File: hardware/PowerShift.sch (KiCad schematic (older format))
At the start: 64 parts, among them J1 Barrel_Jack, J10 SHIFT_IN, J11 JST-ZR, J12 JST-ZR, J14 JST-ZR, J2 MICRO_USB, J3 JST-ZR, J4 JST-ZR, J5 SHIFT_IN, J6 SHIFT_IN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

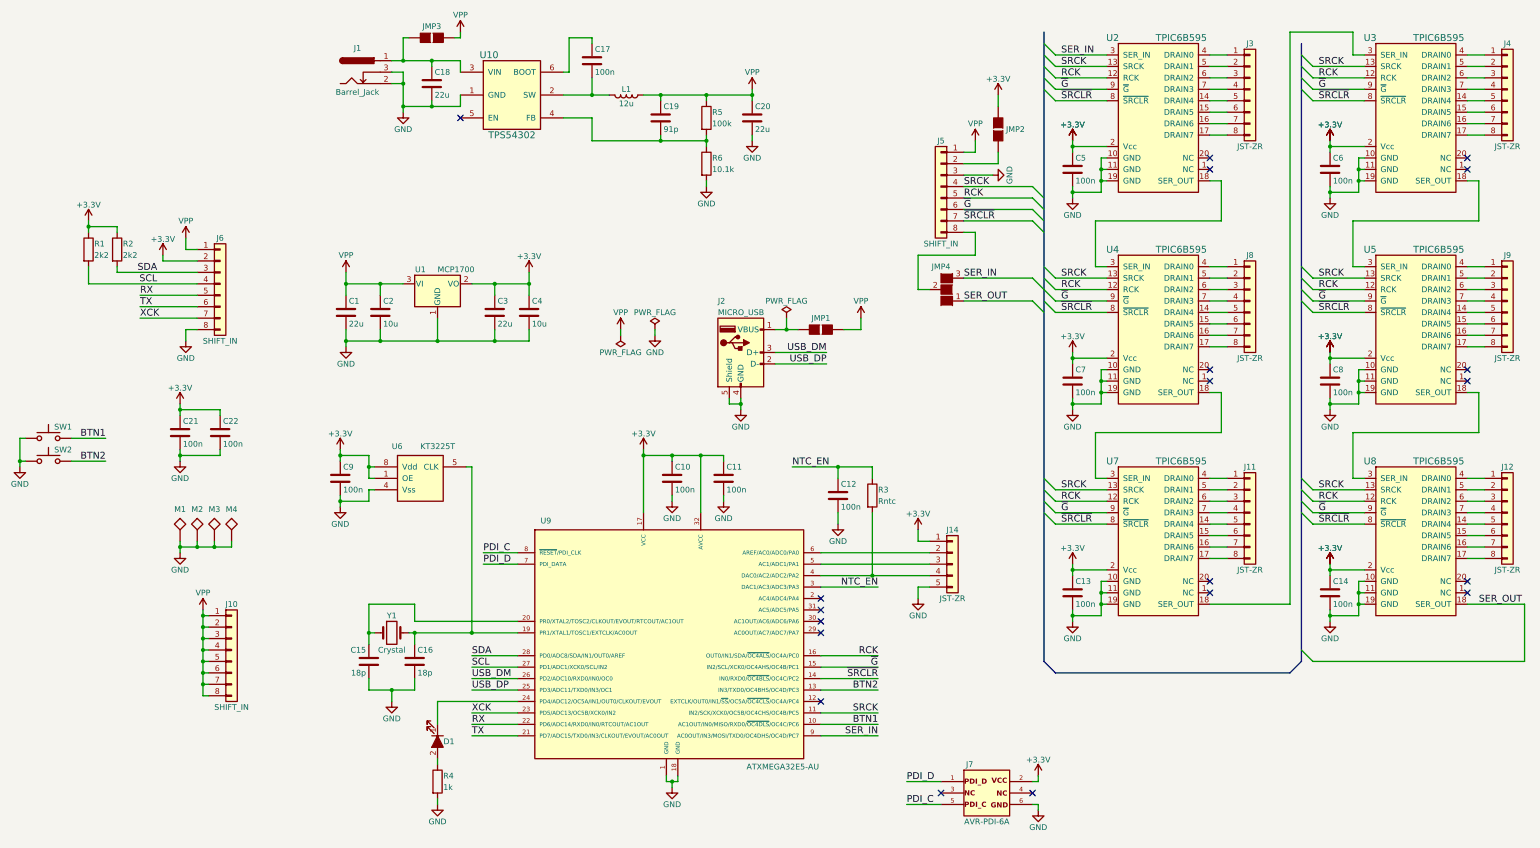
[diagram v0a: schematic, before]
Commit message: Cleaned up schematic layout
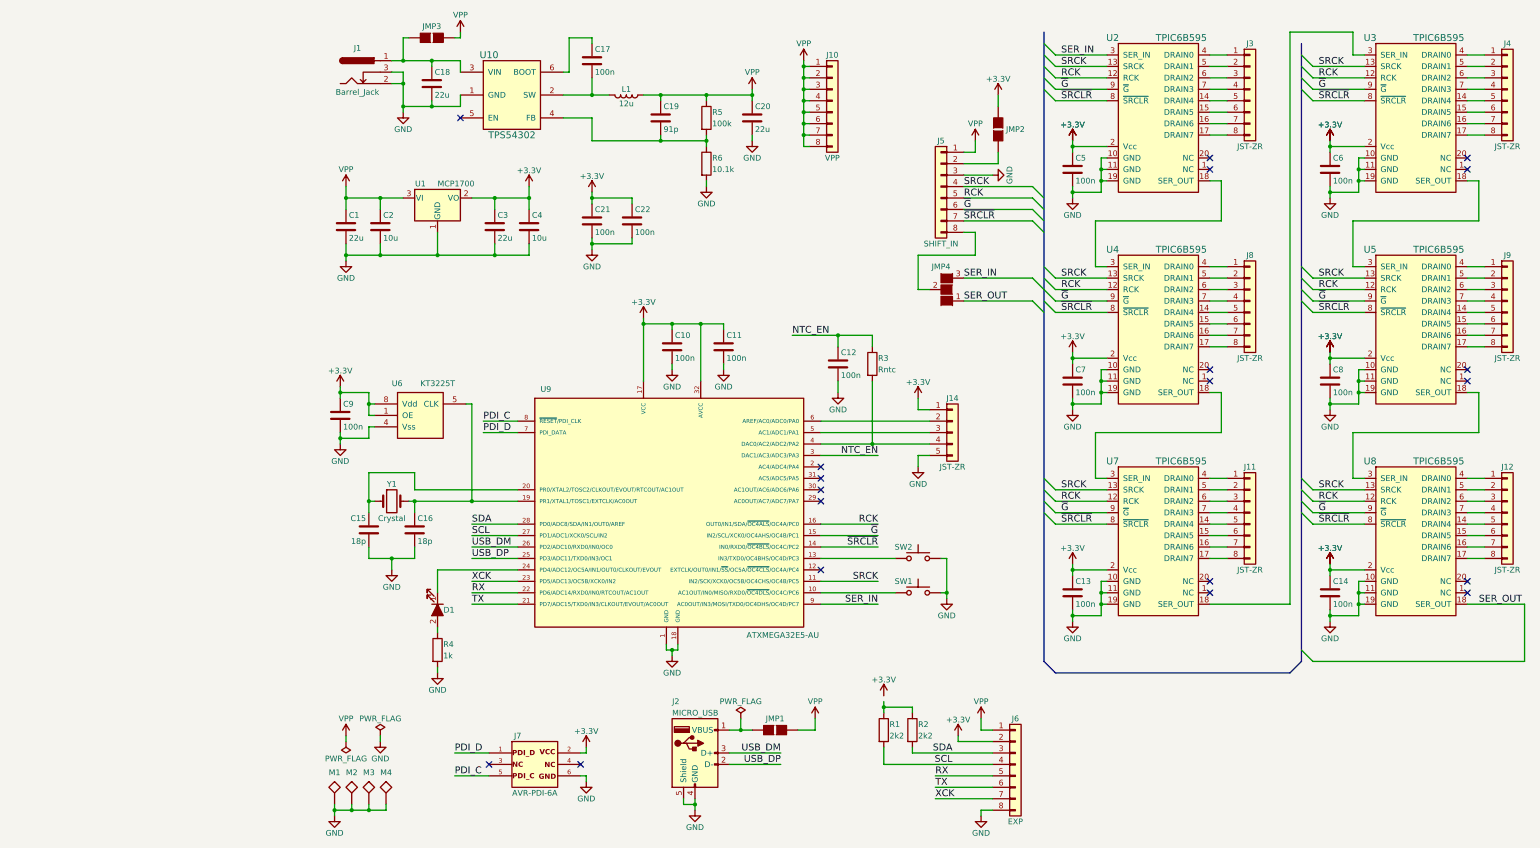
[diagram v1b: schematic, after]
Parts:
- J10: value SHIFT_IN -> VPP
- J6: value SHIFT_IN -> EXP
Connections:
- net +3V3: no longer R1.1, R2.1
- net BTN1: no longer names the net of SW1.2, U9.10 (AC1OUT/IN0/MISO/RXD0/~OC4DLS~/OC4C/PC6)
- net BTN2: no longer names the net of SW2.2, U9.13 (IN3/TXD0/OC4BHS/OC4D/PC3)
- new net: R1.1, R2.1
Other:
- moved on the sheet: C1, C10, C11, C12, C15, C16, C2, C21, C22, C3, C4, C9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

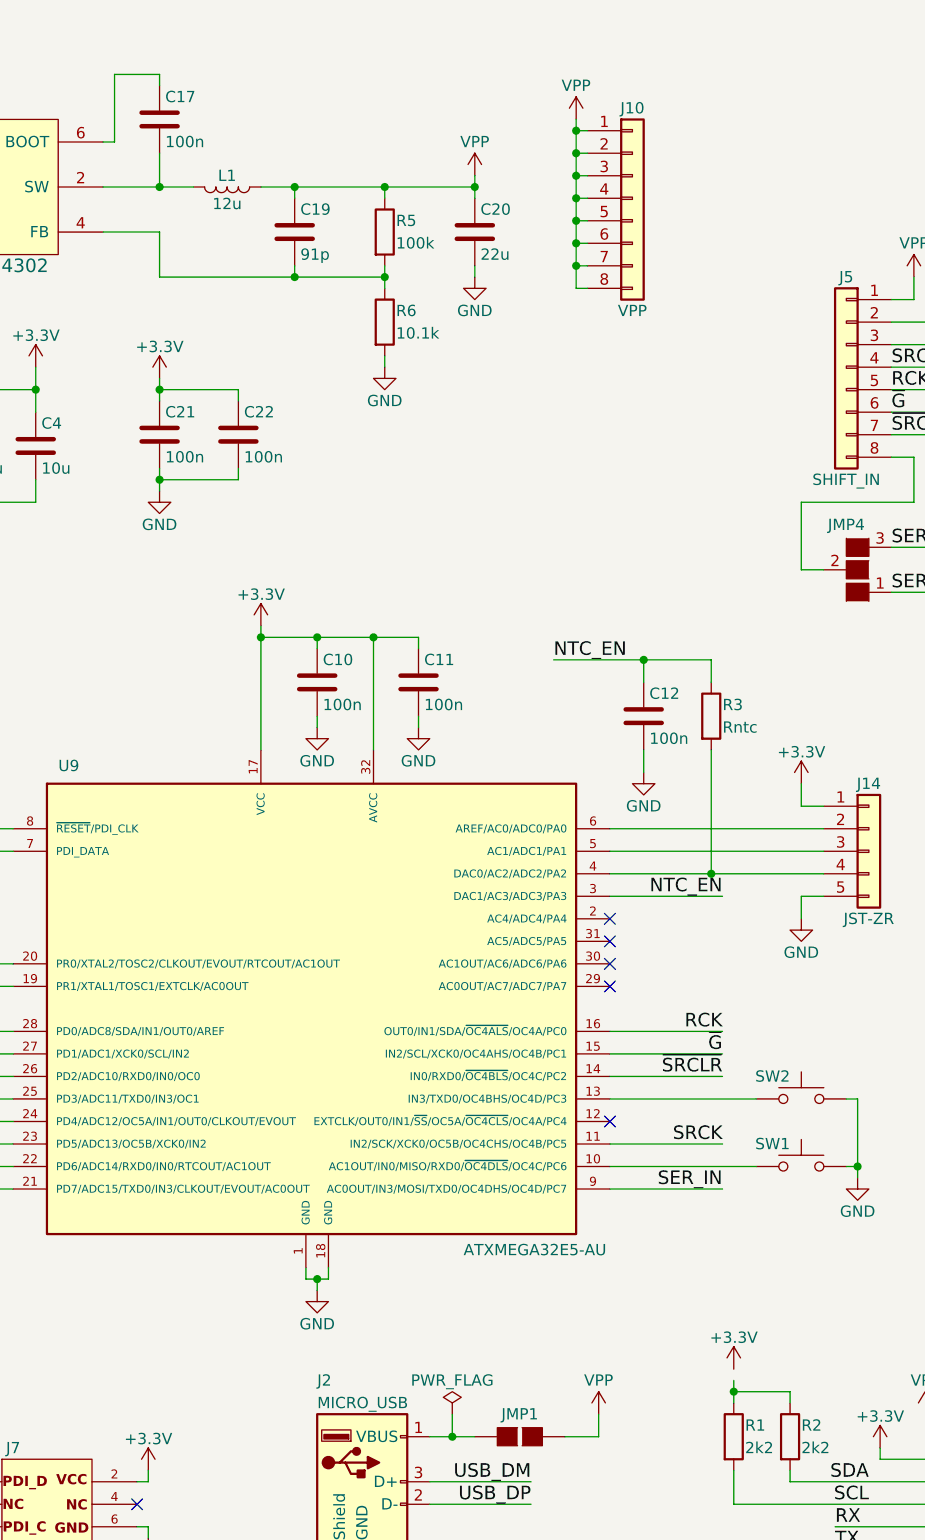
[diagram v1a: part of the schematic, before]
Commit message: Added Vpp voltage switch
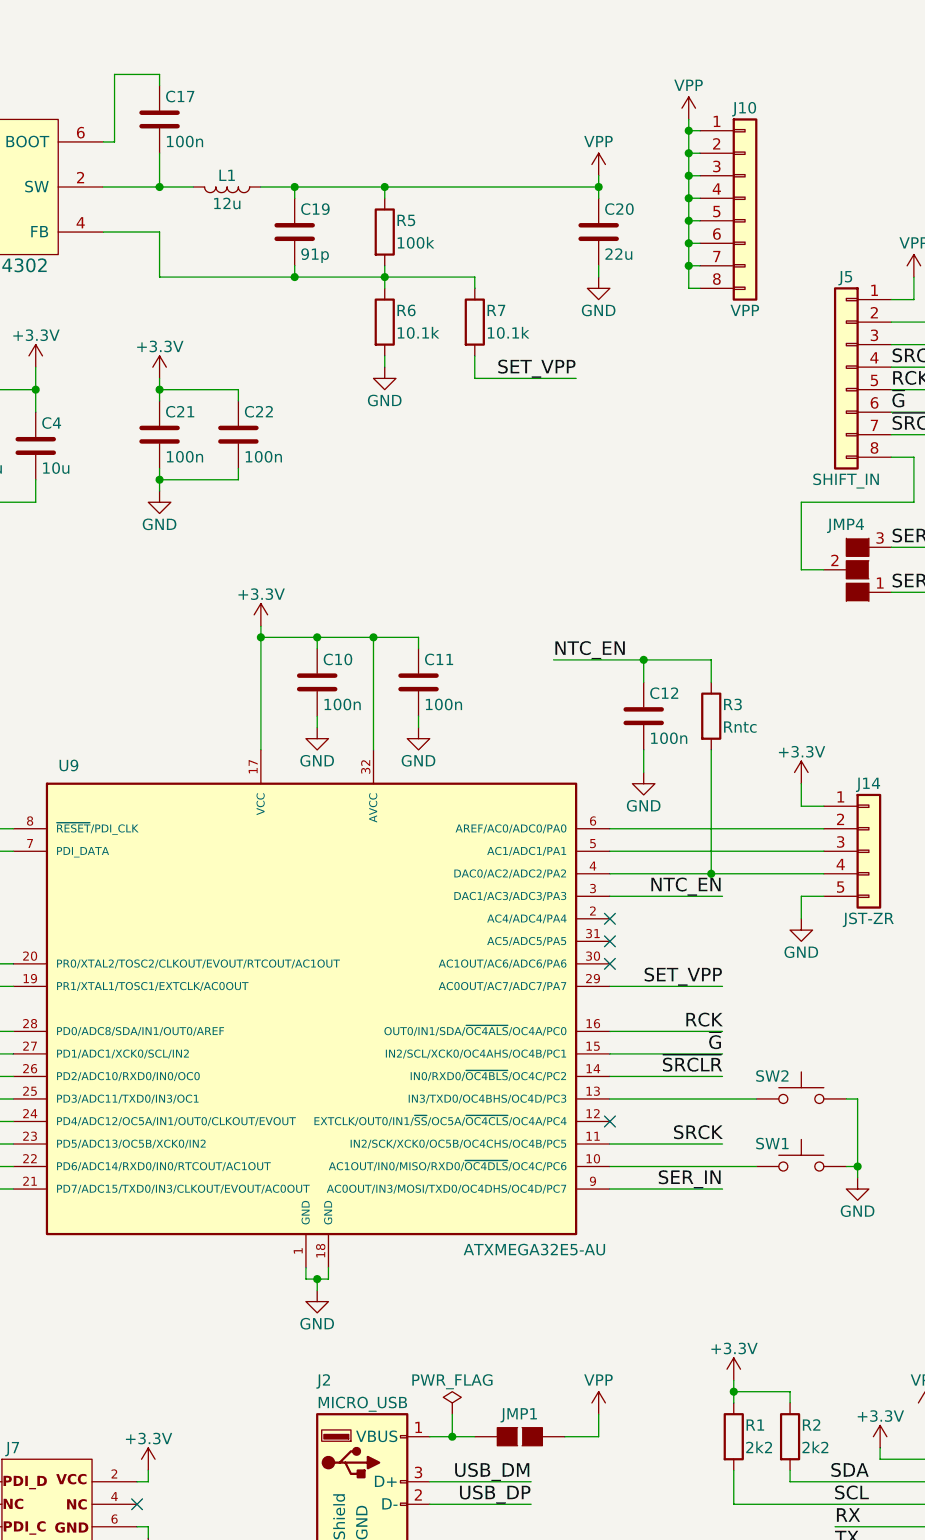
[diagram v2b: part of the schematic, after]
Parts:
- added R7: 10.1k, Resistors_SMD:R_0603_HandSoldering, symbol R
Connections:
- net +3V3: now also R1.1, R2.1
- net SET_VPP: now reaches U9.29 (AC0OUT/AC7/ADC7/PA7)
- net SET_VPP: now also R7.2
- net at C19.2, R5.2, R6.1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: now also R7.1
- no-connect marks 20 -> 19
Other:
- moved on the sheet: C20, J10
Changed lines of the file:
@@
 L VPP #PWR04
 U 1 1 5B2FD383
-P 4250 1200
-F 0 "#PWR04" H 4250 1050 50  0001 C CNN
-F 1 "VPP" H 4250 1350 50  0000 C CNN
-F 2 "" H 4250 1200 50  0001 C CNN
-F 3 "" H 4250 1200 50  0001 C CNN
-	1    4250 1200
+P 4800 1200
+F 0 "#PWR04" H 4800 1050 50  0001 C CNN
+F 1 "VPP" H 4800 1350 50  0000 C CNN
+F 2 "" H 4800 1200 50  0001 C CNN
+F 3 "" H 4800 1200 50  0001 C CNN
+	1    4800 1200
 	1    0    0    -1
 $EndComp
@@
 L +3.3V #PWR038
 U 1 1 5B320992
-P 5400 6500
-F 0 "#PWR038" H 5400 6350 50  0001 C CNN
-F 1 "+3.3V" H 5400 6640 50  0000 C CNN
-F 2 "" H 5400 6500 50  0001 C CNN
-F 3 "" H 5400 6500 50  0001 C CNN
-	1    5400 6500
+P 5400 6550
+F 0 "#PWR038" H 5400 6400 50  0001 C CNN
+F 1 "+3.3V" H 5400 6690 50  0000 C CNN
+F 2 "" H 5400 6550 50  0001 C CNN
+F 3 "" H 5400 6550 50  0001 C CNN
+	1    5400 6550
 	1    0    0    -1
 $EndComp
@@
 NoConn ~ 4850 4600
 NoConn ~ 4850 4700
-NoConn ~ 4850 4800
 NoConn ~ 4850 5400
 Entry Wire Line
@@
 L C C20
 U 1 1 5B314AC7
-P 4250 1450
-F 0 "C20" H 4275 1550 50  0000 L CNN
-F 1 "22u" H 4275 1350 50  0000 L CNN
-F 2 "Capacitors_SMD:C_0805_HandSoldering" H 4288 1300 50  0001 C CNN
-F 3 "" H 4250 1450 50  0001 C CNN
-	1    4250 1450
+P 4800 1450
+F 0 "C20" H 4825 1550 50  0000 L CNN
+F 1 "22u" H 4825 1350 50  0000 L CNN
+F 2 "Capacitors_SMD:C_0805_HandSoldering" H 4838 1300 50  0001 C CNN
+F 3 "" H 4800 1450 50  0001 C CNN
+	1    4800 1450
 	1    0    0    -1
 $EndComp
@@
 Connection ~ 2850 1250
 Wire Wire Line
-	3300 1250 4250 1250
+	3300 1250 4800 1250
 Wire Wire Line
 	3450 1250 3450 1300
@@
 Connection ~ 1200 1350
 Wire Wire Line
-	2850 1650 3850 1650
-Wire Wire Line
-	4250 1200 4250 1300
+	2850 1650 4250 1650
+Wire Wire Line
+	4800 1200 4800 1300
 Connection ~ 3850 1250
-Connection ~ 4250 1250
+Connection ~ 4800 1250
 $Comp
 L GND #PWR049
@@
 L GND #PWR050
 U 1 1 5B319B94
-P 4250 1650
-F 0 "#PWR050" H 4250 1400 50  0001 C CNN
-F 1 "GND" H 4250 1500 50  0000 C CNN
-F 2 "" H 4250 1650 50  0001 C CNN
-F 3 "" H 4250 1650 50  0001 C CNN
-	1    4250 1650
-	1    0    0    -1
-$EndComp
-Wire Wire Line
-	4250 1650 4250 1600
+P 4800 1650
+F 0 "#PWR050" H 4800 1400 50  0001 C CNN
+F 1 "GND" H 4800 1500 50  0000 C CNN
+F 2 "" H 4800 1650 50  0001 C CNN
+F 3 "" H 4800 1650 50  0001 C CNN
+	1    4800 1650
+	1    0    0    -1
+$EndComp
+Wire Wire Line
+	4800 1650 4800 1600
 NoConn ~ 1700 1450
 $Comp
@@
 L Conn_01x08 J10
 U 1 1 5B33885D
-P 4950 1300
-F 0 "J10" H 4950 1700 50  0000 C CNN
-F 1 "VPP" H 4950 800 50  0000 C CNN
-F 2 "kuro:B8B-ZR-SM4-TF" H 4950 1300 50  0001 C CNN
-F 3 "" H 4950 1300 50  0001 C CNN
-	1    4950 1300
+P 5450 1300
+F 0 "J10" H 5450 1700 50  0000 C CNN
+F 1 "VPP" H 5450 800 50  0000 C CNN
+F 2 "kuro:B8B-ZR-SM4-TF" H 5450 1300 50  0001 C CNN
+F 3 "" H 5450 1300 50  0001 C CNN
+	1    5450 1300
 	1    0    0    -1
 $EndComp
@@
 L VPP #PWR055
 U 1 1 5B338DC5
-P 4700 950
-F 0 "#PWR055" H 4700 800 50  0001 C CNN
-F 1 "VPP" H 4700 1100 50  0000 C CNN
-F 2 "" H 4700 950 50  0001 C CNN
-F 3 "" H 4700 950 50  0001 C CNN
-	1    4700 950
-	1    0    0    -1
-$EndComp
-Wire Wire Line
-	4700 950  4700 1700
-Wire Wire Line
-	4700 1700 4750 1700
-Wire Wire Line
-	4700 1000 4750 1000
-Connection ~ 4700 1000
-Connection ~ 4700 1100
-Connection ~ 4700 1200
-Connection ~ 4700 1300
-Connection ~ 4700 1400
-Connection ~ 4700 1500
-Connection ~ 4700 1600
-Wire Wire Line
-	4700 1100 4750 1100
-Wire Wire Line
-	4700 1200 4750 1200
-Wire Wire Line
-	4700 1300 4750 1300
-Wire Wire Line
-	4700 1400 4750 1400
-Wire Wire Line
-	4700 1500 4750 1500
-Wire Wire Line
-	4700 1600 4750 1600
+P 5200 950
+F 0 "#PWR055" H 5200 800 50  0001 C CNN
+F 1 "VPP" H 5200 1100 50  0000 C CNN
+F 2 "" H 5200 950 50  0001 C CNN
+F 3 "" H 5200 950 50  0001 C CNN
+	1    5200 950
+	1    0    0    -1
+$EndComp
+Wire Wire Line
+	5200 950  5200 1700
+Wire Wire Line
+	5200 1700 5250 1700
+Wire Wire Line
+	5200 1000 5250 1000
+Connection ~ 5200 1000
+Connection ~ 5200 1100
+Connection ~ 5200 1200
+Connection ~ 5200 1300
+Connection ~ 5200 1400
+Connection ~ 5200 1500
+Connection ~ 5200 1600
+Wire Wire Line
+	5200 1100 5250 1100
+Wire Wire Line
+	5200 1200 5250 1200
+Wire Wire Line
+	5200 1300 5250 1300
+Wire Wire Line
+	5200 1400 5250 1400
+Wire Wire Line
+	5200 1500 5250 1500
+Wire Wire Line
+	5200 1600 5250 1600
 $Comp
 L SW_Push SW1
@@
 Wire Wire Line
 	6250 7550 6250 7500
+$Comp
+L R R7
+U 1 1 5B42671E
+P 4250 1850
+F 0 "R7" H 4300 1900 50  0000 L CNN
+F 1 "10.1k" H 4300 1800 50  0000 L CNN
+F 2 "Resistors_SMD:R_0603_HandSoldering" V 4180 1850 50  0001 C CNN
+F 3 "" H 4250 1850 50  0001 C CNN
+	1    4250 1850
+	1    0    0    -1
+$EndComp
+Wire Wire Line
+	4250 1650 4250 1700
+Wire Wire Line
+	4250 2000 4250 2100
+Wire Wire Line
+	4250 2100 4700 2100
+Text Label 4700 2100 2    60   ~ 0
+SET_VPP
+Text Label 5350 4800 2    60   ~ 0
+SET_VPP
+Wire Wire Line
+	4850 4800 5350 4800
 $EndSCHEMATC
